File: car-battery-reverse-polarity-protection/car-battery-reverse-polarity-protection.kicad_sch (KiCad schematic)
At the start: 5 parts, among them J1 Battery Connector, J2 Output, K1 Relay_SPDT

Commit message: PCB layout rev 1 complete.
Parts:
- added H1, H2, H3: MountingHole_Pad, MountingHole:MountingHole_3.2mm_M3_Pad, symbol Mechanical:MountingHole_Pad
- added H4: Logo, ProjectLibrary:rocketry_logo_small_noletters, symbol Mechanical:MountingHole
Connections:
- net GND: now also H1.1, H2.1, H3.1

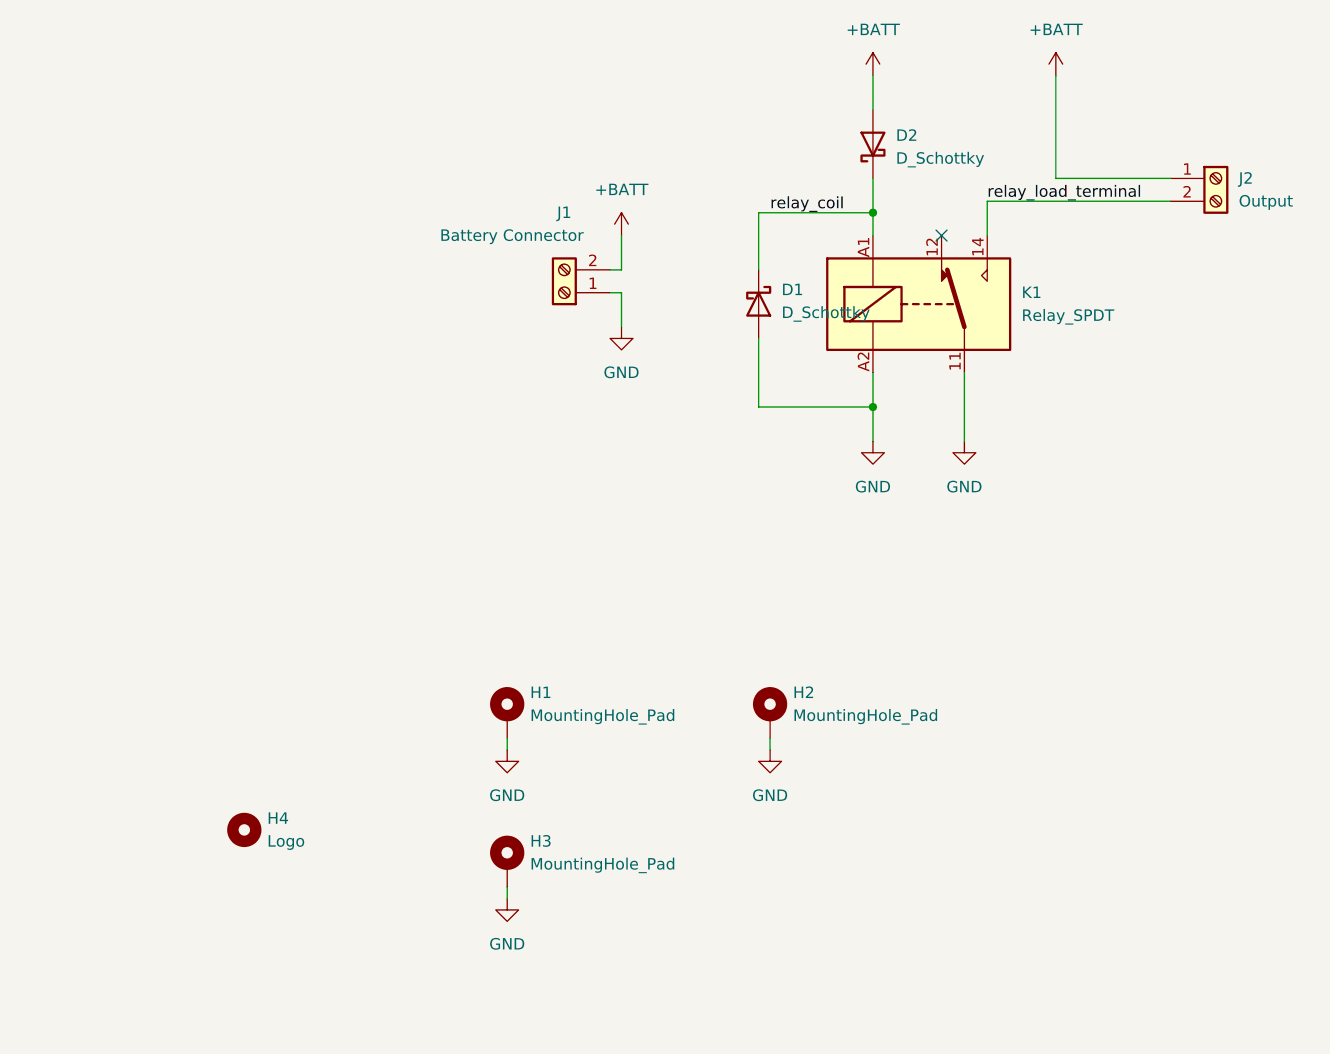
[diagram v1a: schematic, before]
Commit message: PCB and schematic changes:
- Made board and power traces bigger to meet current requirements.
- Standardized silkscreen labels.
- Updated component values in schematic.
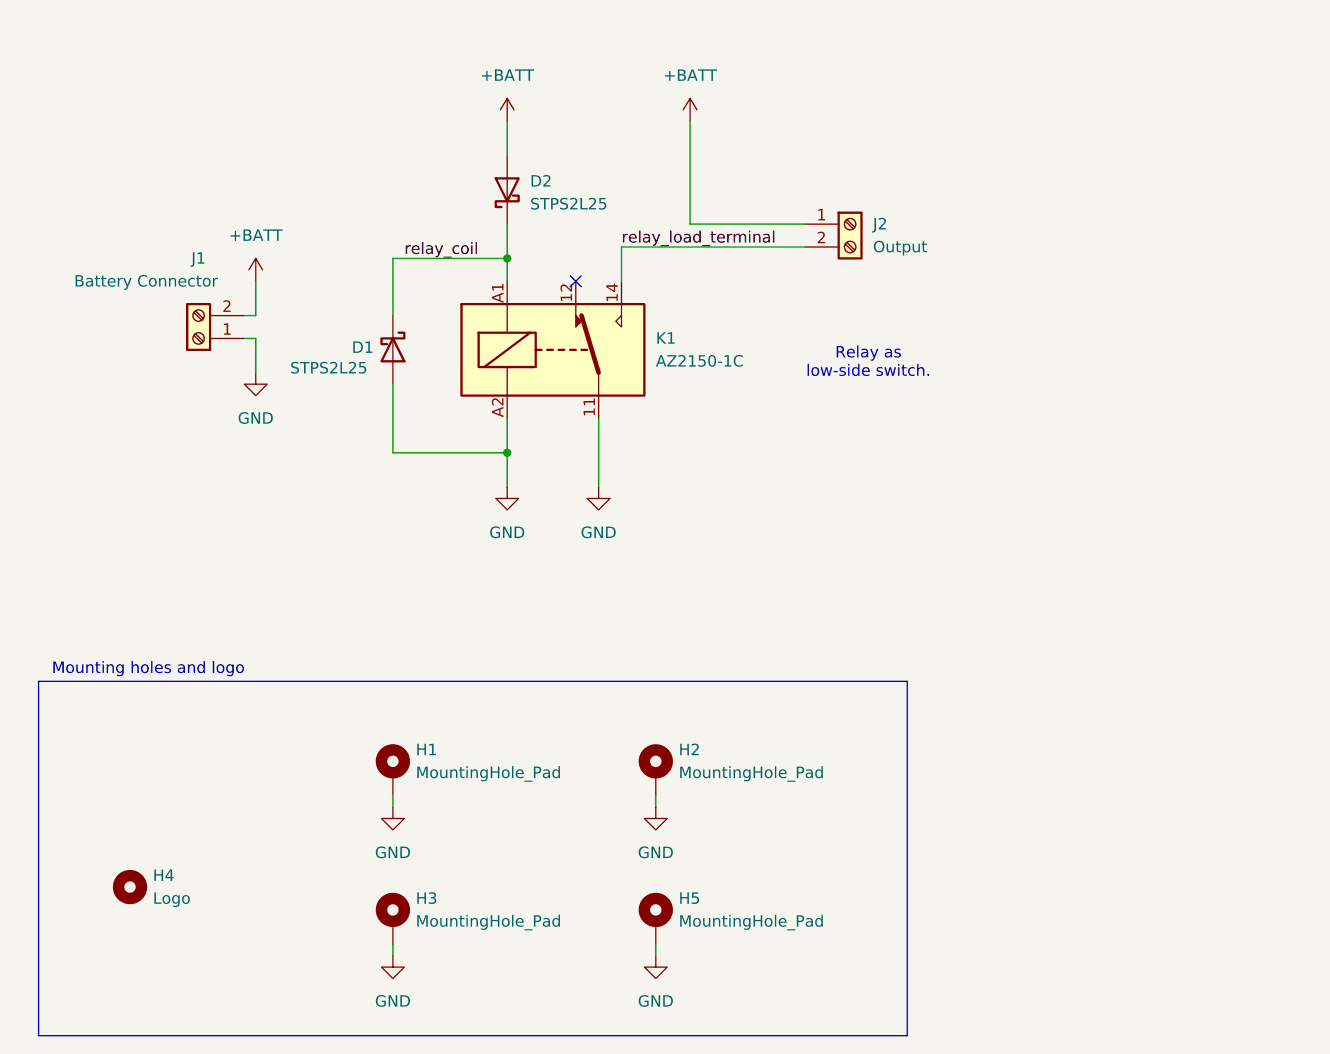
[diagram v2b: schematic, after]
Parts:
- added H5: MountingHole_Pad, MountingHole:MountingHole_3.2mm_M3_Pad, symbol Mechanical:MountingHole_Pad
- D1, D2: value D_Schottky -> STPS2L25
- K1: value Relay_SPDT -> AZ2150-1C
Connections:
- net GND: now also H5.1
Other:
- note added: "Mounting holes and logo"
- note added: "Relay as low-side switch."
- company: (none) -> Waterloo Rocketry
- title: (none) -> Tank Heating 24VDC Reverse Voltage Protection
- moved on the sheet: D1, D2, H1, H2, H3, H4, J1, J2, K1

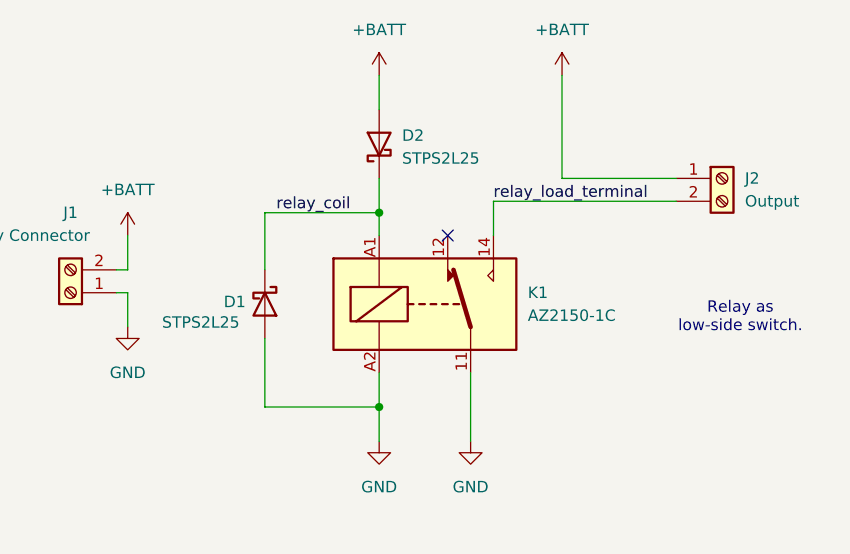
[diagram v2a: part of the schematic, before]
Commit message: Updates RE: PR
- Updated diode and relay part numbers.
- Updated relay symbol.

Size of board dictated by mounting hole requirement:
- x distance between holes 37mm
- y distance 65 mm
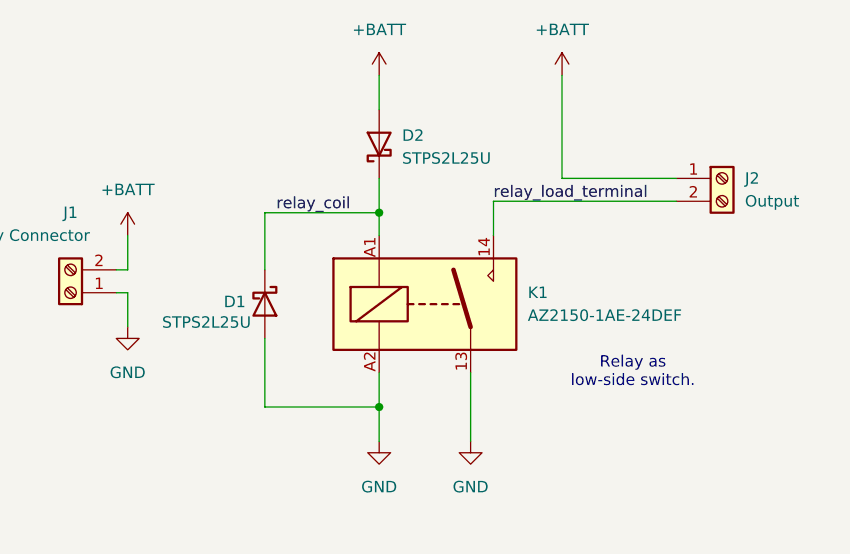
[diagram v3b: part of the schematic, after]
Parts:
- removed K1: AZ2150-1C, ProjectLibrary:AZ2150_AMZ, symbol Relay:Relay_SPDT
- added K1: AZ2150-1AE-24DEF, ProjectLibrary:AZ2150_AMZ, symbol Relay:Relay_SPST-NO
- D1, D2: value STPS2L25 -> STPS2L25U
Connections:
- net GND: now also K1.13, K1.A2
- net relay_coil: now also K1.A1
- net relay_load_terminal: now also K1.14
- no-connect marks 1 -> 0
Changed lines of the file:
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@@
 		(color 0 0 0 0)
-	)
-	(no_connect
-		(at 146.05 80.01)
 	)
 	(wire
@@
 	(text "Relay as\nlow-side switch."
 		(exclude_from_sim no)
-		(at 178.562 89.154 0)
+		(at 166.624 95.25 0)
 		(effects
 			(font
@@
 			)
 		)
-		(property "Value" "STPS2L25"
+		(property "Value" "STPS2L25U"
 			(at 114.3 89.662 90)
 			(effects
@@
 			)
 		)
-		(property "Description" "Schottky diode"
+		(property "Description" "Schottky diode."
 			(at 125.73 87.63 0)
 			(effects
@@
 	)
 	(symbol
-		(lib_id "Relay:Relay_SPDT")
+		(lib_id "power:GND")
+		(at 110.49 90.17 0)
+		(unit 1)
+		(exclude_from_sim no)
+		(in_bom yes)
+		(on_board yes)
+		(dnp no)
+		(fields_autoplaced yes)
+		(property "Reference" "#PWR03"
+			(at 110.49 96.52 0)
+			(effects
+				(font
+					(size 1.27 1.27)
+				)
+				(hide yes)
+			)
+		)
+		(property "Value" "GND"
+			(at 110.49 95.25 0)
+			(effects
+				(font
+					(size 1.27 1.27)
+				)
+			)
+		)
+		(property "Footprint" ""
+			(at 110.49 90.17 0)
+			(effects
+				(font
+					(size 1.27 1.27)
+				)
+				(hide yes)
+			)
+		)
+		(property "Datasheet" ""
+			(at 110.49 90.17 0)
+			(effects
+				(font
+					(size 1.27 1.27)
+				)
+				(hide yes)
+			)
+		)
+		(property "Description" "Power symbol creates a global label with name \"GND\" , ground"
+			(at 110.49 90.17 0)
+			(effects
+				(font
+					(size 1.27 1.27)
+				)
+				(hide yes)
+			)
+		)
+		(pin "1"
+		)
+		(instances
+			(project ""
+				(path "/749bcb34-7dfb-46c1-ab6d-e6eff02c90ec"
+					(reference "#PWR03")
+					(unit 1)
+				)
+			)
+		)
+	)
+	(symbol
+		(lib_id "power:GND")
+		(at 154.94 154.94 0)
+		(unit 1)
+		(exclude_from_sim no)
+		(in_bom yes)
+		(on_board yes)
+		(dnp no)
+		(fields_autoplaced yes)
+		(property "Reference" "#PWR010"
+			(at 154.94 161.29 0)
+			(effects
+				(font
+					(size 1.27 1.27)
+				)
+				(hide yes)
+			)
+		)
+		(property "Value" "GND"
+			(at 154.94 160.02 0)
+			(effects
+				(font
+					(size 1.27 1.27)
+				)
+			)
+		)
+		(property "Footprint" ""
+			(at 154.94 154.94 0)
+			(effects
+				(font
+					(size 1.27 1.27)
+				)
+				(hide yes)
+			)
+		)
+		(property "Datasheet" ""
+			(at 154.94 154.94 0)
+			(effects
+				(font
+					(size 1.27 1.27)
+				)
+				(hide yes)
+			)
+		)
+		(property "Description" "Power symbol creates a global label with name \"GND\" , ground"
+			(at 154.94 154.94 0)
+			(effects
+				(font
+					(size 1.27 1.27)
+				)
+				(hide yes)
+			)
+		)
+		(pin "1"
+		)
+		(instances
+			(project "car-battery-reverse-polarity-protection"
+				(path "/749bcb34-7dfb-46c1-ab6d-e6eff02c90ec"
+					(reference "#PWR010")
+					(unit 1)
+				)
+			)
+		)
+	)
+	(symbol
+		(lib_id "Relay:Relay_SPST-NO")
 		(at 143.51 87.63 0)
 		(unit 1)
@@
 		(on_board yes)
 		(dnp no)
+		(fields_autoplaced yes)
 		(property "Reference" "K1"
 			(at 154.94 86.3599 0)
@@
 			)
 		)
-		(property "Value" "AZ2150-1C"
+		(property "Value" "AZ2150-1AE-24DEF"
 			(at 154.94 88.8999 0)
 			(effects
@@
 			)
 		)
-		(property "Description" "Relay SPDT, monostable, EN50005"
+		(property "Description" "Relay SPST, normally open, EN50005"
 			(at 143.51 87.63 0)
 			(effects
@@
 			)
 		)
-		(pin "11"
-		)
-		(pin "12"
-		)
 		(pin "A1"
 		)
+		(pin "13"
+		)
+		(pin "A2"
+		)
 		(pin "14"
 		)
-		(pin "A2"
-		)
 		(instances
 			(project ""
 				(path "/749bcb34-7dfb-46c1-ab6d-e6eff02c90ec"
 					(reference "K1")
-					(unit 1)
-				)
-			)
-		)
-	)
-	(symbol
-		(lib_id "power:GND")
-		(at 110.49 90.17 0)
-		(unit 1)
-		(exclude_from_sim no)
-		(in_bom yes)
-		(on_board yes)
-		(dnp no)
-		(fields_autoplaced yes)
-		(property "Reference" "#PWR03"
-			(at 110.49 96.52 0)
-			(effects
-				(font
-					(size 1.27 1.27)
-				)
-				(hide yes)
-			)
-		)
-		(property "Value" "GND"
-			(at 110.49 95.25 0)
-			(effects
-				(font
-					(size 1.27 1.27)
-				)
-			)
-		)
-		(property "Footprint" ""
-			(at 110.49 90.17 0)
-			(effects
-				(font
-					(size 1.27 1.27)
-				)
-				(hide yes)
-			)
-		)
-		(property "Datasheet" ""
-			(at 110.49 90.17 0)
-			(effects
-				(font
-					(size 1.27 1.27)
-				)
-				(hide yes)
-			)
-		)
-		(property "Description" "Power symbol creates a global label with name \"GND\" , ground"
-			(at 110.49 90.17 0)
-			(effects
-				(font
-					(size 1.27 1.27)
-				)
-				(hide yes)
-			)
-		)
-		(pin "1"
-		)
-		(instances
-			(project ""
-				(path "/749bcb34-7dfb-46c1-ab6d-e6eff02c90ec"
-					(reference "#PWR03")
-					(unit 1)
-				)
-			)
-		)
-	)
-	(symbol
-		(lib_id "power:GND")
-		(at 154.94 154.94 0)
-		(unit 1)
-		(exclude_from_sim no)
-		(in_bom yes)
-		(on_board yes)
-		(dnp no)
-		(fields_autoplaced yes)
-		(property "Reference" "#PWR010"
-			(at 154.94 161.29 0)
-			(effects
-				(font
-					(size 1.27 1.27)
-				)
-				(hide yes)
-			)
-		)
-		(property "Value" "GND"
-			(at 154.94 160.02 0)
-			(effects
-				(font
-					(size 1.27 1.27)
-				)
-			)
-		)
-		(property "Footprint" ""
-			(at 154.94 154.94 0)
-			(effects
-				(font
-					(size 1.27 1.27)
-				)
-				(hide yes)
-			)
-		)
-		(property "Datasheet" ""
-			(at 154.94 154.94 0)
-			(effects
-				(font
-					(size 1.27 1.27)
-				)
-				(hide yes)
-			)
-		)
-		(property "Description" "Power symbol creates a global label with name \"GND\" , ground"
-			(at 154.94 154.94 0)
-			(effects
-				(font
-					(size 1.27 1.27)
-				)
-				(hide yes)
-			)
-		)
-		(pin "1"
-		)
-		(instances
-			(project "car-battery-reverse-polarity-protection"
-				(path "/749bcb34-7dfb-46c1-ab6d-e6eff02c90ec"
-					(reference "#PWR010")
 					(unit 1)
 				)
@@
 			)
 		)
-		(property "Value" "STPS2L25"
+		(property "Value" "STPS2L25U"
 			(at 140.97 71.4374 90)
 			(effects
@@
 			)
 		)
-		(property "Description" "Schottky diode"
+		(property "Description" "Schottky diode."
 			(at 138.43 69.85 0)
 			(effects
